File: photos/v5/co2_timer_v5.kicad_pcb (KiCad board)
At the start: 2 copper layers, 70 x 50 mm, 61 parts, among them J1 BAT1_9V, J2 SOLENOID, J3 ISP, J4 DISPLAY, J5 DC_9-12V, J6 BAT2_9V, SW1 UP, SW2 SET, U1 ATtiny84A, U2 DS3231M, U3 MCP1703A-3.3, U4 DRV8871, U5 TPS3839G30, U6 74LVC1G123

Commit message: docs(co2-timer): v5 fab package and firmware doc refresh
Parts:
- U5: value TPS3839G30 -> TPS3839K33
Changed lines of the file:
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@@
 			)
 		)
-		(property "Value" "TPS3839G30"
+		(property "Value" "TPS3839K33"
 			(at 0 0 0)
 			(layer "F.Fab")

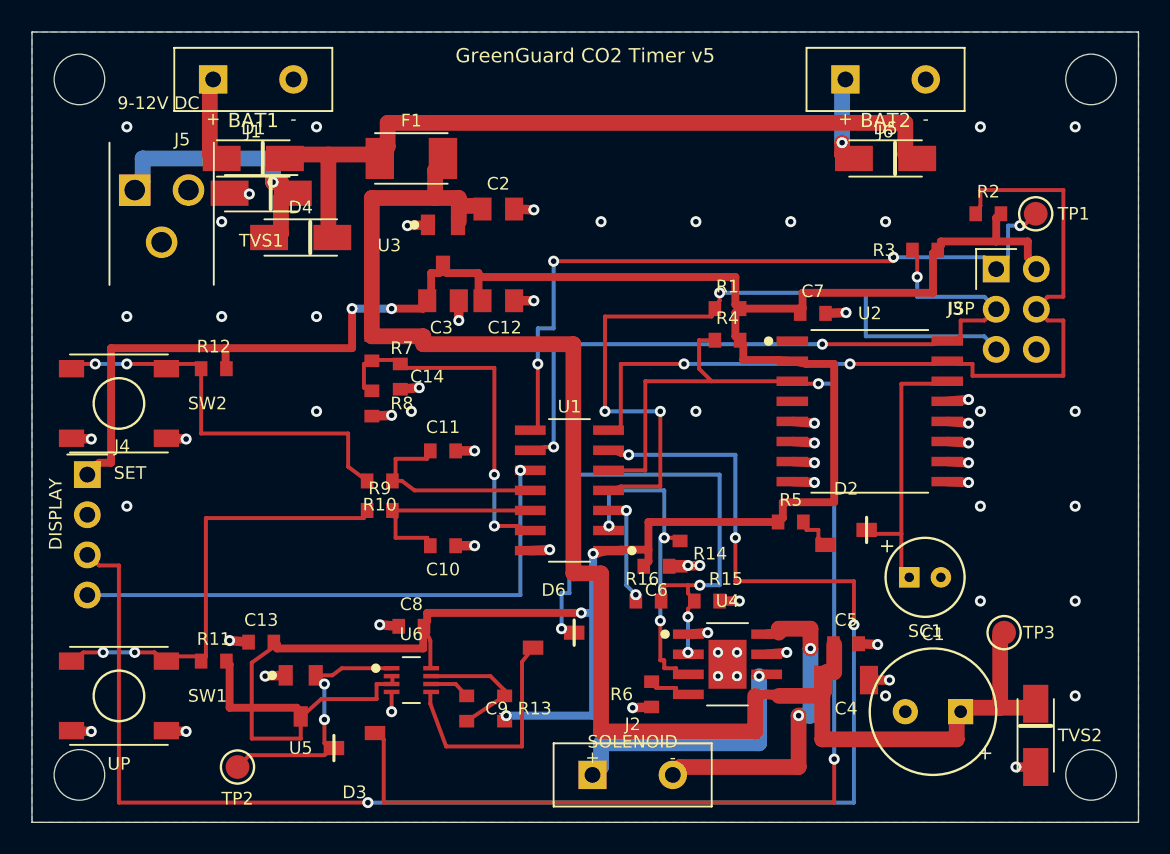
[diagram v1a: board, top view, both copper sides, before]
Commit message: co2-timer v5.1: fail-safe redesign + full adversarial remediation
Adversarial review (2026-08-11) found the shipped-for-quote package had a
reversed regulator pinout, a fail-safe chain that could not actuate (supervisor
tripped 3.5 V below bridge UVLO; one-shot mistimed and self-powered; 470 uF
reservoir off by 100x), unmountable C1/SC1/diode footprints, and no valve spec.

Rev 5.1, verified through six adversarial re-review rounds to RELEASE:
- TPS3700 supervisor on VM (180K/10K, trip 7.50 V) + dual SN74LVC1G3157 muxes
  force IN1=0/IN2=1 at the bridge on trip; one-shot/diode-OR deleted
- U3 MCP1703A pad nets corrected everywhere incl. pad oracle and symbol
- C1 -> 2x 1000 uF D10/P5.0 (sag support role); SC1 -> 0.1 F coin (CHP5R5L104R);
  D2/D3 SOD-323 lands; BOM/CPL/netlist/oracle consistent (172/172)
- Firmware safety items 1-11: OSF masks, periodic schedule eval, close-on-reset
  + hop rescue w/ hold release on clean pass, tear-safe complement journal with
  break-count validation, BCD validation, sticky faults, 8.2/8.6 V lockout with
  .noinit latch + sleep-hop release, VM-measured alert classification
  (6,492 B, sha256 64b0808e...4453, compiled arduino-cli/ATTinyCore on gg-wsl)
- Valve: leak-qualified 6 V direct-acting micro latching class, MPN frozen at
  FA T0; dummy loads derived from measured coil; enclosure stays 1554C2GY
- Docs: T0-T8 + G1-G3 test series, ENIG finish, regulated-adapter constraint,
  Bittele 100-unit/5-FA-hold scope, fab package rebuilt with production hex
  + SHA256SUMS
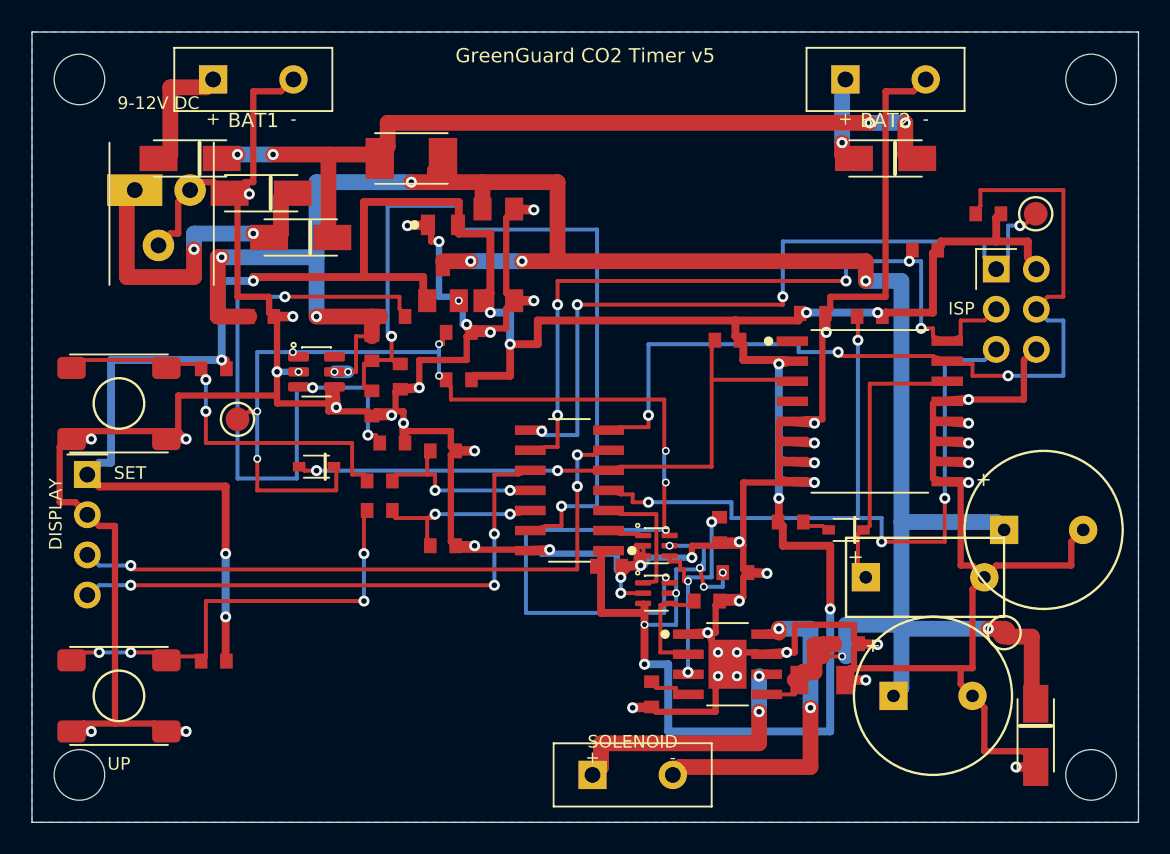
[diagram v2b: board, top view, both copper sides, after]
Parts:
- removed C13, C8: 100nF, Capacitor_SMD:C_0603_1608Metric
- removed the C4 at (51.5, 41.0)
- removed the C5 at (51.5, 38.7)
- removed the C9 at (27.5, 42.8)
- removed the R8 at (21.5, 23.5)
- added C19: 1000uF, Capacitor_THT:CP_Radial_D10.0mm_P5.00mm, F.Cu at (64.0, 31.5)
- added R11: 10K, Resistor_SMD:R_0603_1608Metric, F.Cu at (11.5, 39.8)
- added R12: 10K, Resistor_SMD:R_0603_1608Metric, F.Cu at (11.5, 21.3)
- added R16: 10K 1%, Resistor_SMD:R_0603_1608Metric, F.Cu at (22.8, 26.0)
- added R17: 100K, Resistor_SMD:R_0603_1608Metric, F.Cu at (27.0, 19.0)
- added R18: 10K, Resistor_SMD:R_0603_1608Metric, F.Cu at (27.0, 22.0)
- added R9: 100R, Resistor_SMD:R_0603_1608Metric, F.Cu at (22.0, 30.3)
- added U7: 3157_IN2, Package_TO_SOT_SMD:SOT-363_SC-70-6, F.Cu at (39.5, 35.5)
- C1: value 470uF -> 1000uF; footprint Capacitor_THT:CP_Radial_D8.0mm_P3.50mm -> Capacitor_THT:CP_Radial_D10.0mm_P5.00mm
- C14: renamed from R12; value 10K -> 100nF; footprint Resistor_SMD:R_0603_1608Metric -> Capacitor_SMD:C_0603_1608Metric
- C18: renamed from SW1; value UP -> 100nF; footprint Button_Switch_SMD:SW_SPST_SKQG_WithStem -> Capacitor_SMD:C_0603_1608Metric
- C4: renamed from R6; value 43K -> 10uF; footprint Resistor_SMD:R_0603_1608Metric -> Capacitor_SMD:C_1206_3216Metric
- C5: renamed from R14; value 100K -> 100nF; footprint Resistor_SMD:R_0603_1608Metric -> Capacitor_SMD:C_0603_1608Metric
- D2, D3: footprint Package_TO_SOT_SMD:SOT-23 -> Diode_SMD:D_SOD-323
- F1: value PPTC_1.1A -> PPTC 1.1A MF-R110
- J5: footprint Connector_BarrelJack:BarrelJack_CUI_PJ-002A -> co2v5:BarrelJack_CUI_PJ-002A
- R13: value 100K -> 180K 1%
- R15: renamed from D6; value BAT54 -> 100K; footprint Package_TO_SOT_SMD:SOT-23 -> Resistor_SMD:R_0603_1608Metric
- R6: renamed from R16; value 1K -> 43K 1%
- R8: renamed from R11; value 10K -> 33K
- SC1: value 1F_5V5 -> 0.1F_5V5; footprint Capacitor_THT:CP_Radial_D5.0mm_P2.00mm -> co2v5:CP_CHP_10x5_P7.50mm
- SW1: renamed from R9; value 100R -> UP; footprint Resistor_SMD:R_0603_1608Metric -> co2v5:PTS645SM43SMTR92LFS
- SW2: footprint Button_Switch_SMD:SW_SPST_SKQG_WithStem -> co2v5:PTS645SM43SMTR92LFS
- TP2: value /SUPV -> /VM_OK
- U5: value TPS3839K33 -> TPS3700; footprint Package_TO_SOT_SMD:SOT-23 -> Package_TO_SOT_SMD:SOT-23-6
- U6: value 74LVC1G123 -> 3157_IN1; footprint Package_SO:VSSOP-8_2.4x2mm_P0.5mm -> Package_TO_SOT_SMD:SOT-363_SC-70-6
- moved C18 39.8 mm to (44.5, 34.2)
- moved R13 25.8 mm to (22.8, 18.0)
- moved TP2 22.0 mm to (13.0, 24.5)
- moved U5 20.5 mm to (18.0, 21.5)
- moved SW1 20.2 mm to (5.50, 42.0)
- moved R8 19.1 mm to (21.5, 23.5)
- moved D3 18.0 mm to (18.0, 27.5)
- moved U6 17.7 mm to (39.5, 32.5)
- moved C5 11.9 mm to (51.5, 38.7)
- moved C14 11.8 mm to (23.3, 21.8)
- moved C4 10.8 mm to (50.0, 41.0)
- moved R15 9.90 mm to (42.7, 36.0)
- moved C9 9.59 mm to (14.5, 18.0)
- moved R1 9.01 mm to (53.0, 18.0)
- moved R6 5.90 mm to (39.2, 41.9)
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- renumbered C14 to C9, R15 to R14
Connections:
- C14 pad 1: BTN_SET_SW -> VM_SENSE
- C14 pad 2: +3V3 -> GND
- C18 pad 1: BTN_UP_SW -> +3V3
- C18 pad 2: BTN_UP_SW -> GND
- C4 pad 1: ILIM -> VM
- C5 pad 1: DRV_IN1 -> VM
- C9 pad 1: VM_SENSE -> VM
- D3 pad K: /SUPV -> /VM_OK
- R13 pad 1: OS_RC -> VM
- R13 pad 2: +3V3 -> VM_DIV
- R14 pad 1: DRV_IN2 -> DRV_IN1
- R6 pad 1: DRV_IN2_MCU -> ILIM
- R6 pad 2: DRV_IN2 -> GND
- R8 pad 1: BTN_UP_SW -> VM_SENSE
- R8 pad 2: +3V3 -> GND
- SW1 pad 2: BTN_UP -> BTN_UP_SW
- TP2 pad 1: /SUPV -> /VM_OK
- U1 pad 2: DRV_IN1 -> DRV_IN1_MCU
- U3 pad 2: VM -> +3V3
- U3 pad 3: +3V3 -> VM
- U5 pad 1: GND -> /VM_OK
- U5 pad 2: /SUPV -> GND
- U5 pad 3: +3V3 -> VM_DIV
- U6 pad 1: /SUPV -> DRV_IN1_MCU
- U6 pad 2: +3V3 -> GND
- U6 pad 3: +3V3 -> GND
- U6 pad 4: GND -> DRV_IN1
- U6 pad 5: ONESHOT_Q -> +3V3
- U6 pad 6: OS_CEXT -> /VM_OK
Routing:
- net GND: track 47.2 -> 373.7 mm, vias 65 -> 49
- net /VM_OK: track 0.00 -> 86.1 mm, vias 0 -> 9
- net TM_DIO: track 101.3 -> 40.8 mm, vias 4 -> 3
- net VM: track 103.9 -> 153.3 mm, vias 0 -> 10
- net VM_DIV: track 0.00 -> 43.4 mm, vias 0 -> 3
- net /ALERT: track 83.5 -> 42.0 mm
- net VM_SENSE: track 22.8 -> 55.4 mm
- net DRV_IN2: track 36.8 -> 9.06 mm, vias 4 -> 0
- net +3V3: track 190.8 -> 215.6 mm, vias 5 -> 18
- net /SUPV: track 16.9 -> 0.00 mm, vias 2 -> 0
- net ONESHOT_Q: track 14.9 -> 0.00 mm
- net OS_RC: track 8.31 -> 0.00 mm
- net VIN_DC: track 17.4 -> 24.9 mm, vias 1 -> 2
- net /RESET: track 46.6 -> 53.4 mm, vias 3 -> 4
- net VIN_OR: track 49.4 -> 55.3 mm, vias 0 -> 4
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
